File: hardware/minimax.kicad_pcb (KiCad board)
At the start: 2 copper layers, 50 x 50 mm, 5 parts, among them J1 DF37NC-30DS-0.4V_51_, U1 MAX96717GTJ/VY+

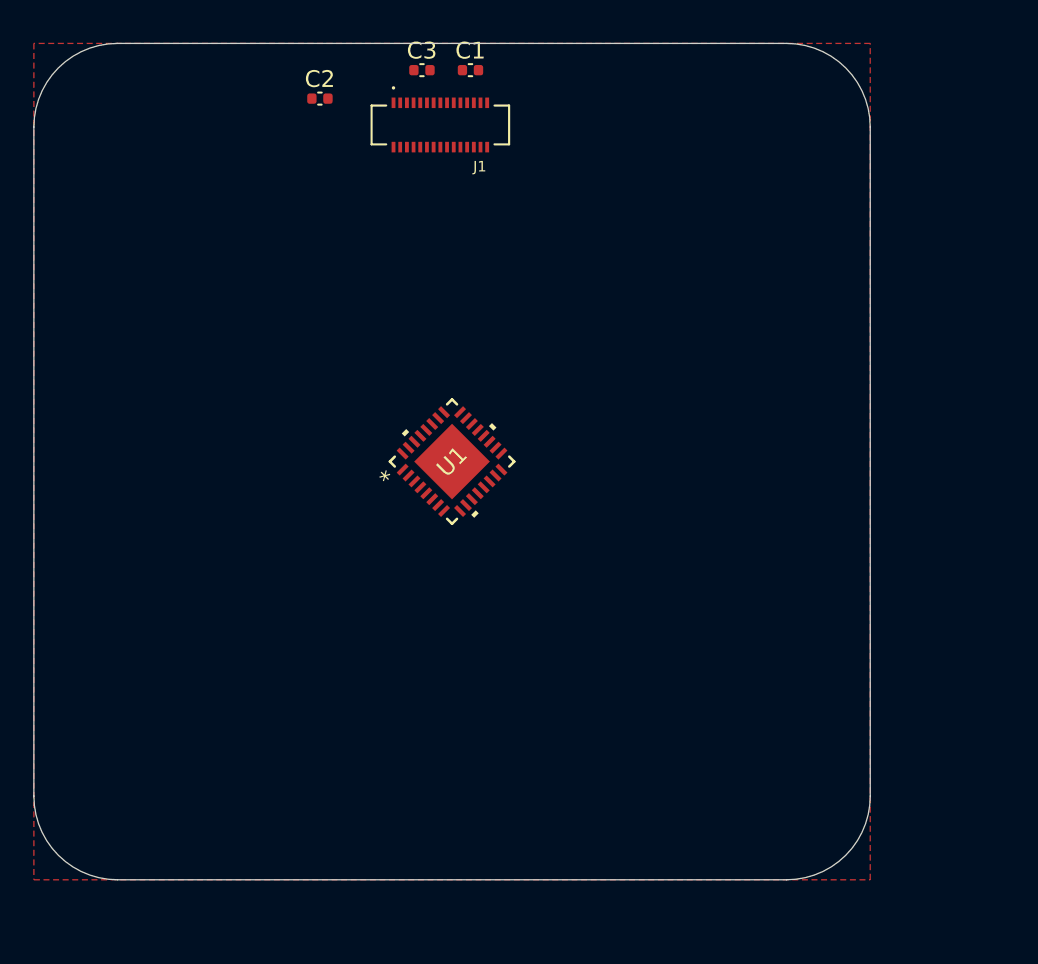
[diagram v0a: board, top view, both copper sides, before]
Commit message: mipi interface land swapping
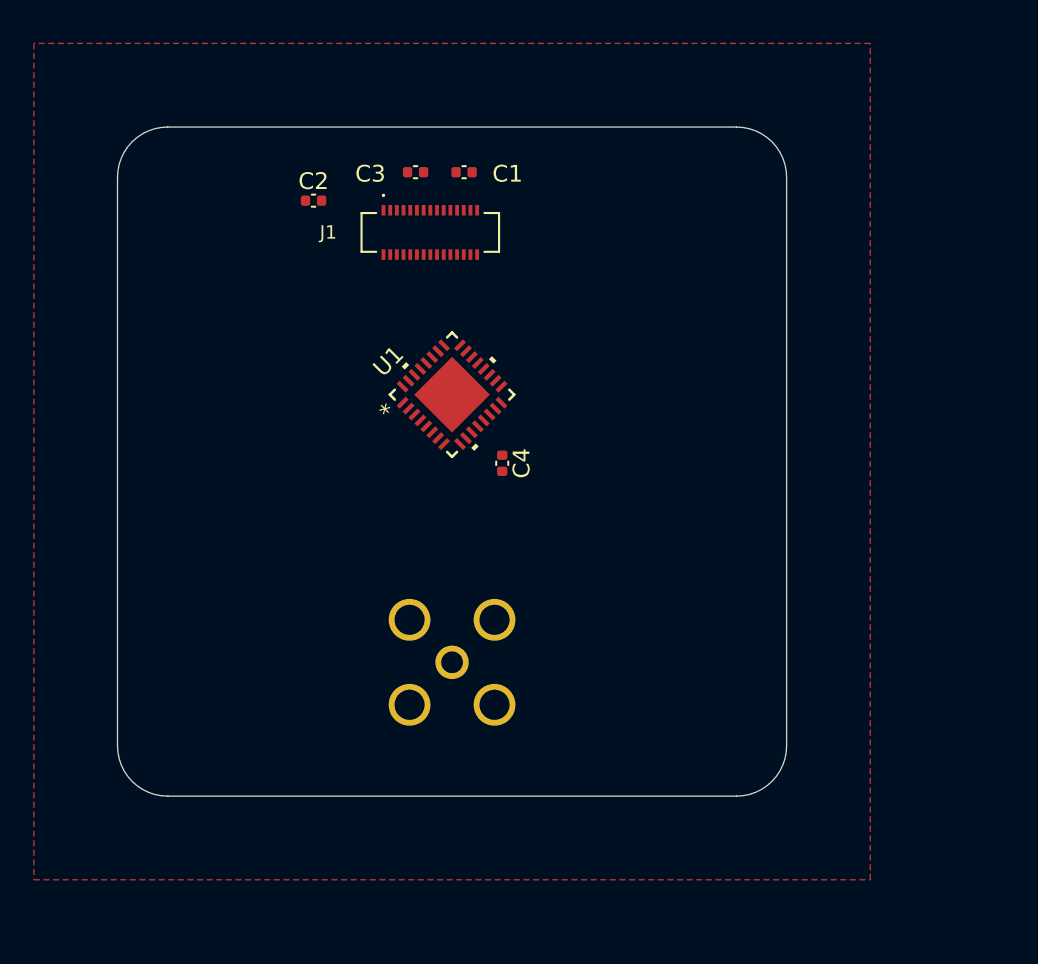
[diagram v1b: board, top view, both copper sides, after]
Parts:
- added C4: 100N, Capacitor_SMD:C_0402_1005Metric, F.Cu at (153.0, 100.1)
- added J2: 2FA1-NZSP-PCBB6, user:2FA1-NZSP-PCBB6, B.Cu at (150.0, 112.0)
- moved J1 6.45 mm to (148.7, 86.3)
- moved C1 6.11 mm to (150.7, 82.7)
- moved C2 6.11 mm to (141.7, 84.4)
- moved C3 6.11 mm to (147.8, 82.7)
- moved U1 4.00 mm to (150.0, 96.0)
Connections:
- U1 pad 12: unconnected-(U1-SIOP-Pad12) -> SIOP
- U1 pad 19: CSI_D2_P -> CSI_D3_N
- U1 pad 20: CSI_D2_N -> CSI_D3_P
- U1 pad 23: CSI_D3_P -> CSI_D2_N
- U1 pad 24: CSI_D3_N -> CSI_D2_P
- U1 pad 25: CSI_D0_P -> CSI_D1_N
- U1 pad 26: CSI_D0_N -> CSI_D1_P
- U1 pad 27: CSI_CLK_P -> CSI_CLK_N
- U1 pad 28: CSI_CLK_N -> CSI_CLK_P
- U1 pad 29: CSI_D1_P -> CSI_D0_N
- U1 pad 30: CSI_D1_N -> CSI_D0_P
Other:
- board size 50 x 50 mm -> 40 x 40 mm

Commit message: cleaned schematics and moving to rpi v2 camera form factor
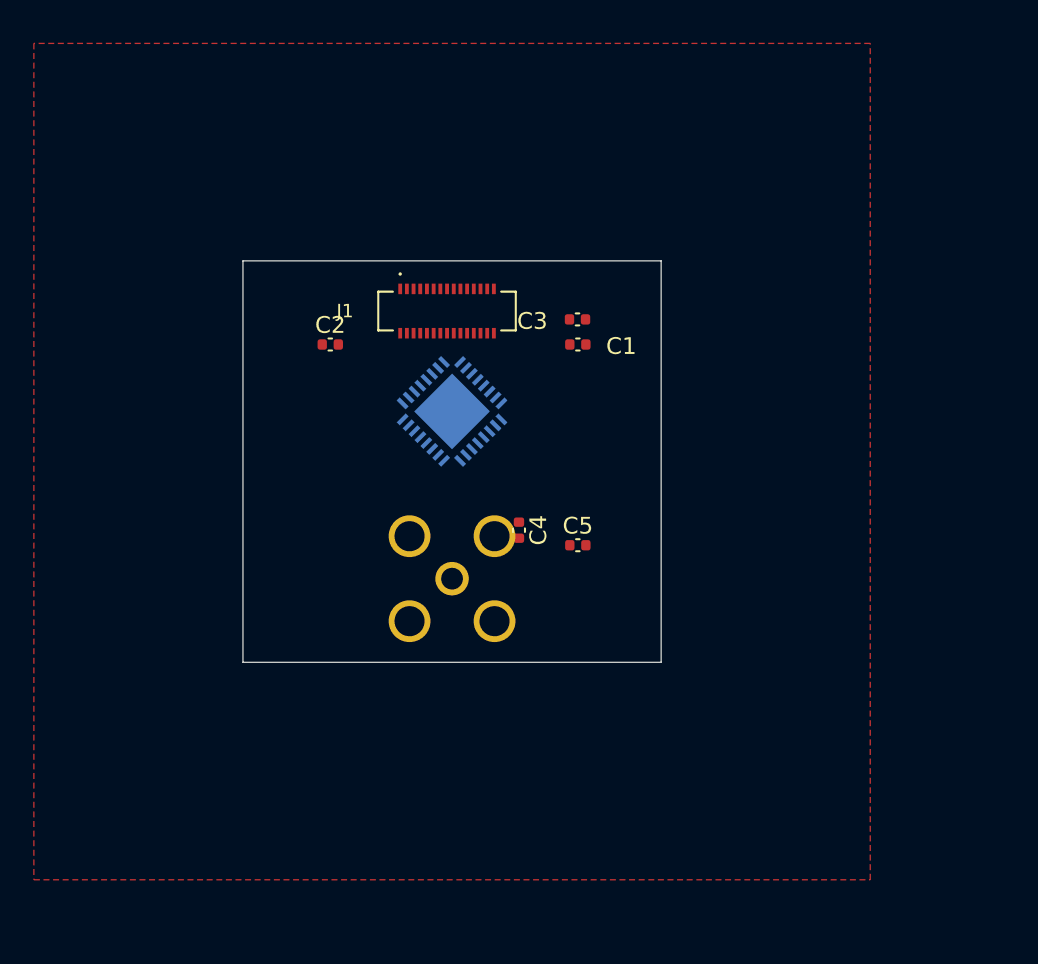
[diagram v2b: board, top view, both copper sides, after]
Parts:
- added C5: 100N, Capacitor_SMD:C_0402_1005Metric, F.Cu at (157.5, 105.0)
- U1: moved to B.Cu
- moved C3 13.1 mm to (157.5, 91.5)
- moved C1 12.3 mm to (157.5, 93.0)
- moved C2 8.66 mm to (142.7, 93.0)
- moved J2 5.00 mm to (150.0, 107.0)
- moved J1 4.81 mm to (149.7, 91.0)
- moved C4 4.12 mm to (154.0, 104.1)
- moved U1 1.00 mm to (150.0, 97.0), turned to 135 degrees
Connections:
- net CSI_CLK_N renamed /camera/MIPI.CSI_CLK_N
- net CSI_CLK_P renamed /camera/MIPI.CSI_CLK_P
- net CSI_D0_N renamed /camera/MIPI.CSI_D0_N
- net CSI_D0_P renamed /camera/MIPI.CSI_D0_P
- net CSI_D1_N renamed /camera/MIPI.CSI_D1_N
- net CSI_D1_P renamed /camera/MIPI.CSI_D1_P
- net CSI_D2_N renamed /camera/MIPI.CSI_D2_N
- net CSI_D2_P renamed /camera/MIPI.CSI_D2_P
- net CSI_D3_N renamed /camera/MIPI.CSI_D3_N
- net CSI_D3_P renamed /camera/MIPI.CSI_D3_P
- net SIOP renamed /connector/SIO_P
- C1 pad 1: +2V8 -> +1V8
- C3 pad 1: +1V8 -> +2V8
- J1 pad 07: MCLK -> /camera/MFP4_RCLKOUT
- J1 pad 29: SCL_1V8 -> /camera/MFP10_SCL
- J1 pad 30: SDA_1V8 -> /camera/MFP9_SDA
- U1 pad 13: unconnected-(U1-SION-Pad13) -> /connector/SIO_N
- U1 pad 18: unconnected-(U1-MFP4-Pad18) -> /camera/MFP4_RCLKOUT
- U1 pad 5: unconnected-(U1-MFP9-Pad5) -> /camera/MFP9_SDA
- U1 pad 6: unconnected-(U1-MFP10-Pad6) -> /camera/MFP10_SCL
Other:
- board size 40 x 40 mm -> 25 x 24 mm

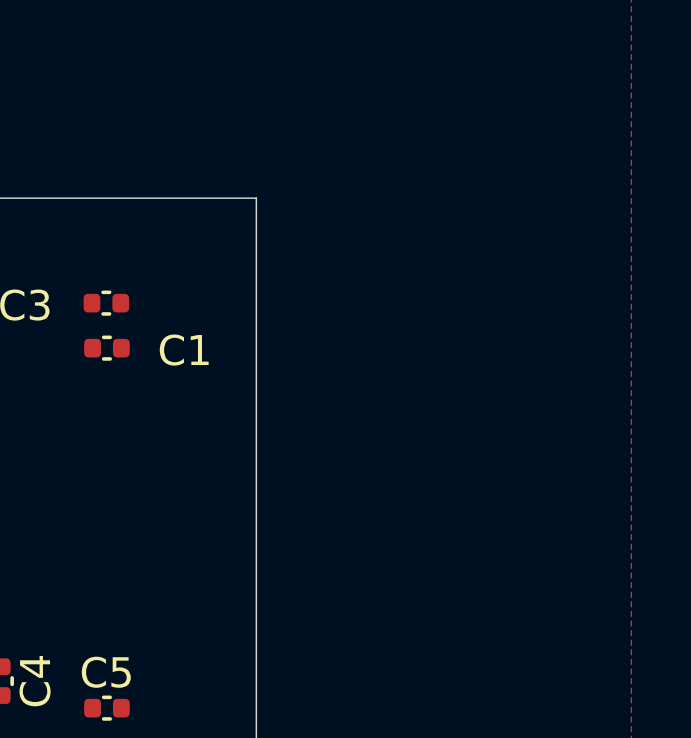
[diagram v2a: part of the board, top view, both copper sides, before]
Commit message: finished rough pass on max96717, need cfgs. added notes to imx219 inck tolerance.
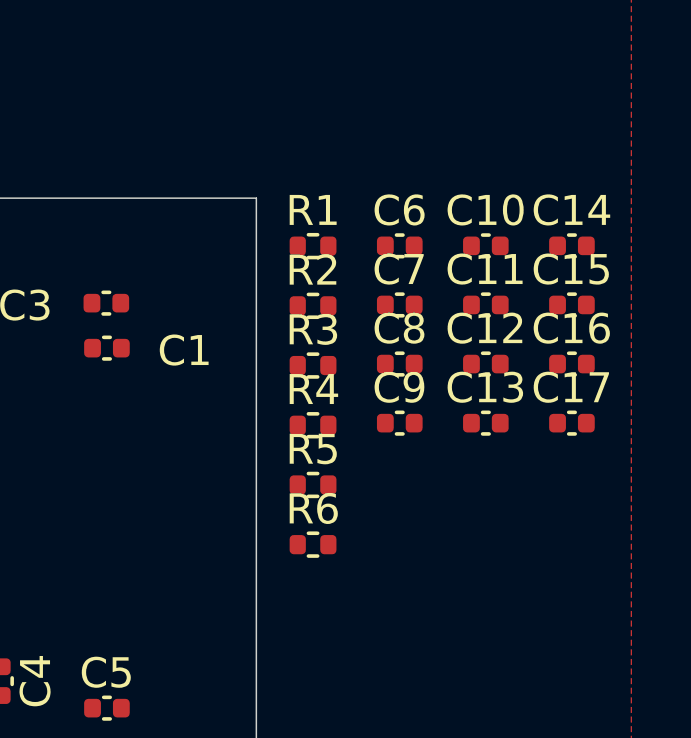
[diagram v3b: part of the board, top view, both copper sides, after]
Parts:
- added C10: 100N, Capacitor_SMD:C_0402_1005Metric, F.Cu at (170.2, 89.6)
- added C11: 10N, Capacitor_SMD:C_0402_1005Metric, F.Cu at (170.2, 91.6)
- added C12: 10U, Capacitor_SMD:C_0402_1005Metric, F.Cu at (170.2, 93.5)
- added C13: 100N, Capacitor_SMD:C_0402_1005Metric, F.Cu at (170.2, 95.5)
- added C14: 10N, Capacitor_SMD:C_0402_1005Metric, F.Cu at (173.0, 89.6)
- added C15: 10U, Capacitor_SMD:C_0402_1005Metric, F.Cu at (173.0, 91.6)
- added C16: 100N, Capacitor_SMD:C_0402_1005Metric, F.Cu at (173.0, 93.5)
- added C17: 10N, Capacitor_SMD:C_0402_1005Metric, F.Cu at (173.0, 95.5)
- added C6: 10U, Capacitor_SMD:C_0402_1005Metric, F.Cu at (167.3, 89.6)
- added C7: 100N, Capacitor_SMD:C_0402_1005Metric, F.Cu at (167.3, 91.6)
- added C8: 10N, Capacitor_SMD:C_0402_1005Metric, F.Cu at (167.3, 93.5)
- added C9: 10U, Capacitor_SMD:C_0402_1005Metric, F.Cu at (167.3, 95.5)
- added R1: 402, Resistor_SMD:R_0402_1005Metric, F.Cu at (164.4, 89.6)
- added R2: 10K, Resistor_SMD:R_0402_1005Metric, F.Cu at (164.4, 91.6)
- added R3: 402, Resistor_SMD:R_0402_1005Metric, F.Cu at (164.4, 93.6)
- added R4: 402, Resistor_SMD:R_0402_1005Metric, F.Cu at (164.4, 95.6)
- added R5: 402, Resistor_SMD:R_0402_1005Metric, F.Cu at (164.4, 97.6)
- added R6: 402, Resistor_SMD:R_0402_1005Metric, F.Cu at (164.4, 99.5)
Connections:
- U1 pad 1: unconnected-(U1-PWDNB-Pad1) -> Net-(U1-PWDNB)
- U1 pad 10: unconnected-(U1-XRES-Pad10) -> Net-(U1-XRES)
- U1 pad 11: unconnected-(U1-VDD18-Pad11) -> VDD18
- U1 pad 14: unconnected-(U1-CAP_VDD-Pad14) -> Net-(U1-CAP_VDD)
- U1 pad 15: unconnected-(U1-VDD-Pad15) -> VDD
- U1 pad 16: unconnected-(U1-VDDIO-Pad16) -> VDDIO
- U1 pad 17: unconnected-(U1-MFP3-Pad17) -> MFP3
- U1 pad 2: unconnected-(U1-MFP0-Pad2) -> MFP0
- U1 pad 21: unconnected-(U1-MFP5-Pad21) -> MFP5
- U1 pad 22: unconnected-(U1-MFP6-Pad22) -> MFP6
- U1 pad 3: unconnected-(U1-MFP1/CFG0-Pad3) -> MFP2_CFG1
- U1 pad 31: unconnected-(U1-MFP7-Pad31) -> MFP7
- U1 pad 32: unconnected-(U1-MFP8-Pad32) -> MFP8
- U1 pad 4: unconnected-(U1-MFP2/CFG1-Pad4) -> MFP1_CFG0

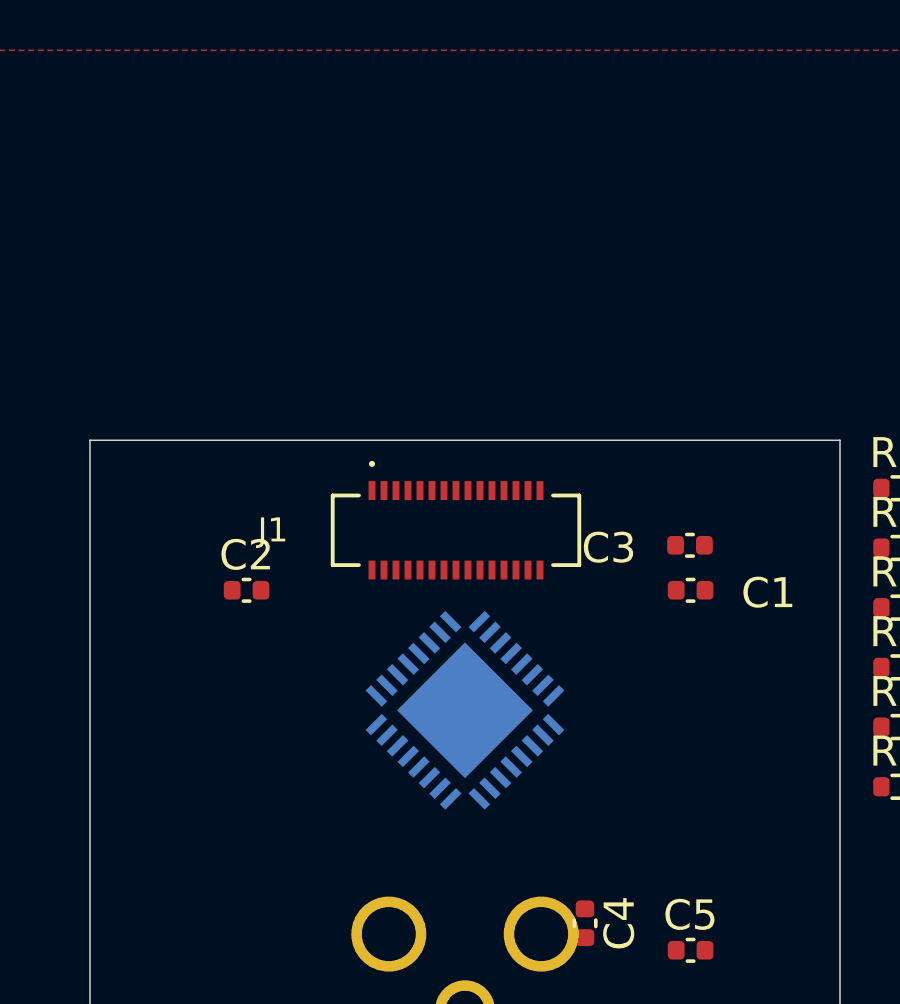
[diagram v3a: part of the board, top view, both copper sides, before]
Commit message: added 22-pin 524352271, need to change fakra to smt
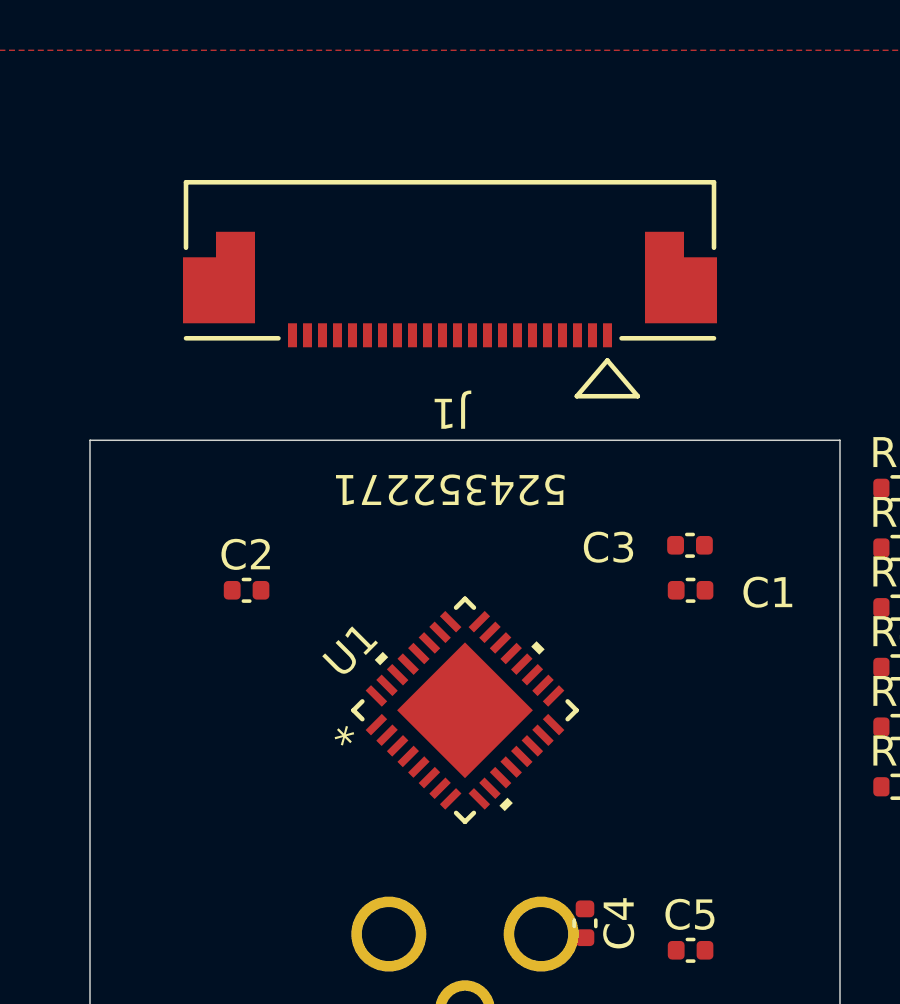
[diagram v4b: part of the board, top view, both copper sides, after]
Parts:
- J1: value DF37NC-30DS-0.4V_51_ -> 524352271; footprint user:HRS_DF37NC-30DS-0.4V_51_ -> user:CON_524352271_MOL
- U1: moved to F.Cu
- moved J1 9.00 mm to (149.5, 82.0)
- turned U1 to 45 degrees
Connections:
- J1 pad 10: +2V8 -> unconnected-(J1-Pad10)
- J1 pad 12: GND -> unconnected-(J1-Pad12)
- J1 pad 13: /camera/MIPI.CSI_D3_P -> unconnected-(J1-Pad13)
- J1 pad 14: /camera/MIPI.CSI_D3_N -> unconnected-(J1-Pad14)
- J1 pad 15: GND -> unconnected-(J1-Pad15)
- J1 pad 16: GND -> unconnected-(J1-Pad16)
- J1 pad 17: /camera/MIPI.CSI_D2_N -> unconnected-(J1-Pad17)
- J1 pad 18: /camera/MIPI.CSI_D2_P -> unconnected-(J1-Pad18)
- J1 pad 19: GND -> unconnected-(J1-Pad19)
- J1 pad 20: /camera/MIPI.CSI_D1_N -> unconnected-(J1-Pad20)
- J1 pad 21: /camera/MIPI.CSI_D1_P -> unconnected-(J1-Pad21)
- J1 pad 22: GND -> unconnected-(J1-Pad22)

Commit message: cleaned up schematics
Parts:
- removed C15: 10U, Capacitor_SMD:C_0402_1005Metric
- added L1: PFL1005-561MRW, user:L_Coilcraft_1210POC, F.Cu at (167.7, 106.6)
- added L2: PFL1005-561MRW, user:L_Coilcraft_PFL1005, F.Cu at (171.5, 109.5)
- added R10: 49.9R, Resistor_SMD:R_0402_1005Metric, F.Cu at (171.7, 107.5)
- added R7: 10K, Resistor_SMD:R_0402_1005Metric, F.Cu at (166.6, 113.5)
- added R8: 10K, Resistor_SMD:R_0402_1005Metric, F.Cu at (166.6, 115.5)
- added R9: 5.1K, Resistor_SMD:R_0402_1005Metric, F.Cu at (171.7, 105.5)
- added REF**: MountingHole_2.2mm_M2, MountingHole:MountingHole_2.2mm_M2, F.Cu at (160.5, 97.5)
- added REF**: MountingHole_2.2mm_M2, MountingHole:MountingHole_2.2mm_M2, F.Cu at (160.5, 109.9)
- added REF**: MountingHole_2.2mm_M2, MountingHole:MountingHole_2.2mm_M2, F.Cu at (139.5, 97.5)
- added REF**: MountingHole_2.2mm_M2, MountingHole:MountingHole_2.2mm_M2, F.Cu at (139.5, 109.9)
- C14: value 10N -> 10U
- R3, R4: value 402 -> 10K
- R5: value 402 -> 32.4K
- R6: value 402 -> 68.1K
- moved C2 26.2 mm to (167.5, 84.5)
- moved C3 16.3 mm to (172.5, 85.0)
- moved C4 15.7 mm to (168.5, 98.0)
- moved C5 14.9 mm to (171.5, 100.0)
- moved J2 11.0 mm to (150.0, 118.0)
- moved C1 10.2 mm to (165.0, 86.0)
- moved J1 8.61 mm to (150.0, 90.6)
- moved U1 4.12 mm to (151.3, 100.9), turned to 0 degrees
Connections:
- net /camera/MFP4_RCLKOUT renamed MFP4
- C14 pad 1: Net-(U1-CAP_VDD) -> unconnected-(C14-Pad1)
- C5 pad 2: unconnected-(C5-Pad2) -> Net-(C5-Pad2)
- C6 pad 1: VDDIO -> unconnected-(C6-Pad1)
- C9 pad 1: VDD -> unconnected-(C9-Pad1)
- J1 pad 1: unconnected-(J1-Pad1) -> GND
- J1 pad 10: unconnected-(J1-Pad10) -> GND
- J1 pad 11: unconnected-(J1-Pad11) -> /camera/MIPI.CSI_D2_N
- J1 pad 12: unconnected-(J1-Pad12) -> /camera/MIPI.CSI_D2_P
- J1 pad 13: unconnected-(J1-Pad13) -> GND
- J1 pad 14: unconnected-(J1-Pad14) -> /camera/MIPI.CSI_D3_N
- J1 pad 15: unconnected-(J1-Pad15) -> /camera/MIPI.CSI_D3_P
- J1 pad 16: unconnected-(J1-Pad16) -> GND
- J1 pad 17: unconnected-(J1-Pad17) -> /camera/POWER_EN
- J1 pad 18: unconnected-(J1-Pad18) -> /camera/LED_EN
- J1 pad 19: unconnected-(J1-Pad19) -> GND
- J1 pad 2: unconnected-(J1-Pad2) -> /camera/MIPI.CSI_D0_N
- J1 pad 20: unconnected-(J1-Pad20) -> /camera/MFP10_SCL
- J1 pad 21: unconnected-(J1-Pad21) -> /camera/MFP9_SDA
- J1 pad 22: unconnected-(J1-Pad22) -> +3.3V
- J1 pad 3: unconnected-(J1-Pad3) -> /camera/MIPI.CSI_D0_P
- J1 pad 4: unconnected-(J1-Pad4) -> GND
- J1 pad 5: unconnected-(J1-Pad5) -> /camera/MIPI.CSI_D1_N
- J1 pad 6: unconnected-(J1-Pad6) -> /camera/MIPI.CSI_D1_P
- J1 pad 7: unconnected-(J1-Pad7) -> GND
- J1 pad 8: unconnected-(J1-Pad8) -> /camera/MIPI.CSI_CLK_N
- J1 pad 9: unconnected-(J1-Pad9) -> /camera/MIPI.CSI_CLK_P
- J1 pad P1: unconnected-(J1-PadP1) -> GND
- J1 pad P2: unconnected-(J1-PadP2) -> GND
- U1 pad 19: /camera/MIPI.CSI_D3_N -> /camera/MIPI.CSI_D2_P
- U1 pad 20: /camera/MIPI.CSI_D3_P -> /camera/MIPI.CSI_D2_N
- U1 pad 23: /camera/MIPI.CSI_D2_N -> /camera/MIPI.CSI_D3_P
- U1 pad 24: /camera/MIPI.CSI_D2_P -> /camera/MIPI.CSI_D3_N
- U1 pad 25: /camera/MIPI.CSI_D1_N -> /camera/MIPI.CSI_D0_P
- U1 pad 26: /camera/MIPI.CSI_D1_P -> /camera/MIPI.CSI_D0_N
- U1 pad 27: /camera/MIPI.CSI_CLK_N -> /camera/MIPI.CSI_CLK_P
- U1 pad 28: /camera/MIPI.CSI_CLK_P -> /camera/MIPI.CSI_CLK_N
- U1 pad 29: /camera/MIPI.CSI_D0_N -> /camera/MIPI.CSI_D1_P
- U1 pad 3: MFP2_CFG1 -> MFP1_CFG0
- U1 pad 30: /camera/MIPI.CSI_D0_P -> /camera/MIPI.CSI_D1_N
- U1 pad 4: MFP1_CFG0 -> MFP2_CFG1
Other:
- board size 25 x 24 mm -> 25 x 35 mm
